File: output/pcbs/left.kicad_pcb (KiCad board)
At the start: 2 copper layers, 123.1 x 95.2 mm, 40 parts

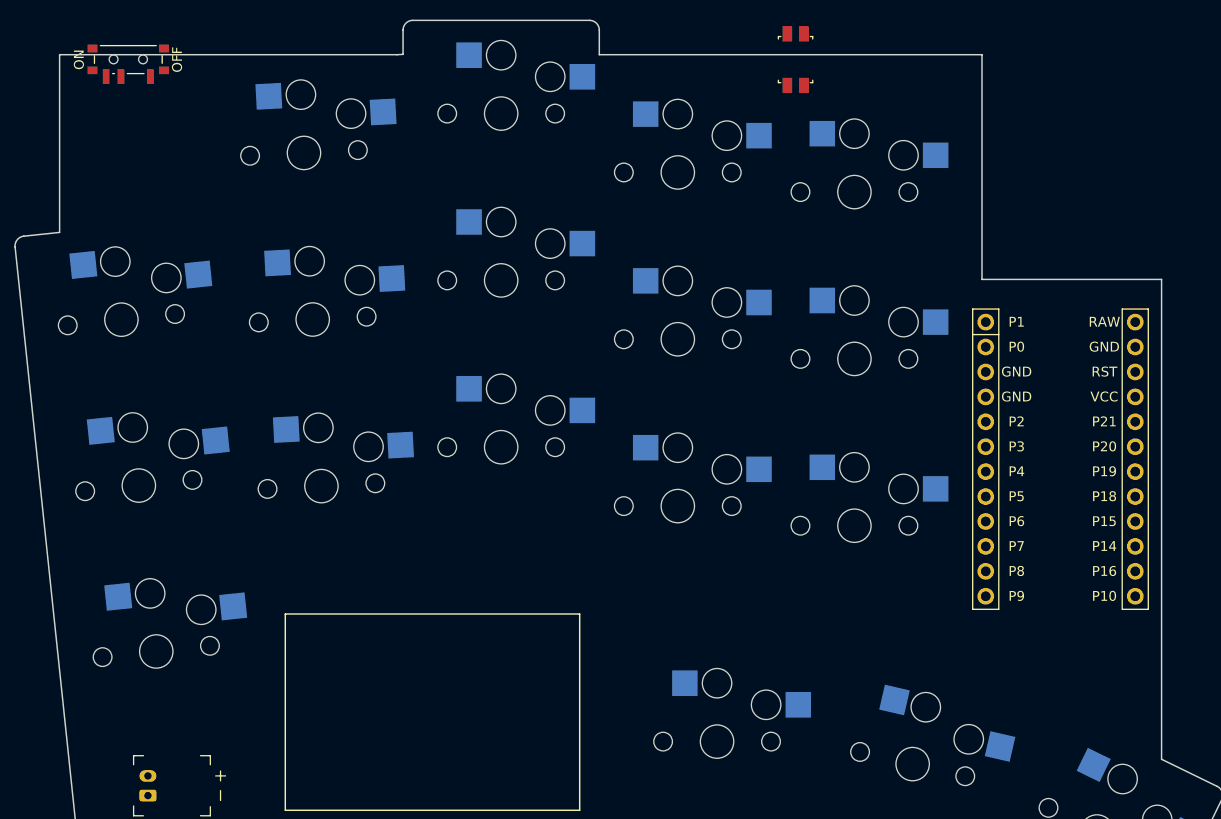
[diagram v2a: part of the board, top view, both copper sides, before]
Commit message: More detailed outlines of power, reset
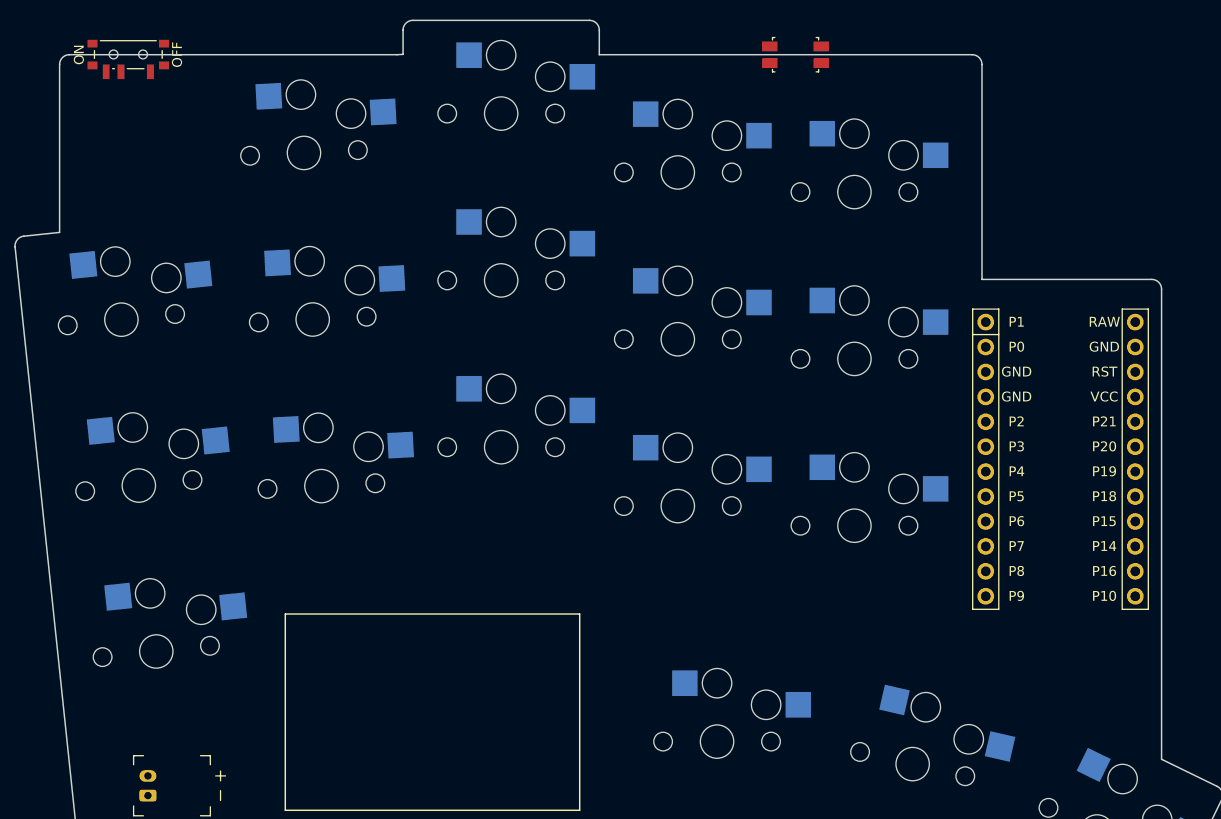
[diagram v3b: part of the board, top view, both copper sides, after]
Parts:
- moved PWR1 0.50 mm to (-2.85, -60.8)
- moved RST1 0.50 mm to (65.1, -60.8), turned to 0 degrees
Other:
- outline, holes or cut-outs redrawn
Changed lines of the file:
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@@
   (footprint "ceoloide:reset_switch_smd_side"
     (layer "F.Cu")
-    (at 65.1483667 -60.315708799999996 90)
+    (at 65.1483667 -60.815708799999996 0)
     (property "Reference" "RST1"
-      (at 0 0 90)
+      (at 0 0 0)
       (layer "F.SilkS")
       hide
@@
     (fp_line (start 1.3 -2.75) (end 1.3 -1.75) (stroke (width 0.1) (type solid)) (layer "Dwgs.User"))
     (fp_line (start 2.35 -1.75) (end 2.35 1.75) (stroke (width 0.1) (type solid)) (layer "Dwgs.User"))
-    (pad "1" smd rect (at 2.625 -0.85 270) (size 1.55 1) (layers "F.Cu" "F.Paste" "F.Mask") (net 3 "GND"))
-    (pad "2" smd rect (at 2.625 0.85 270) (size 1.55 1) (layers "F.Cu" "F.Paste" "F.Mask") (net 77 "RST"))
-    (pad "3" smd rect (at -2.625 -0.85 270) (size 1.55 1) (layers "F.Cu" "F.Paste" "F.Mask") (net 3 "GND"))
-    (pad "4" smd rect (at -2.625 0.85 270) (size 1.55 1) (layers "F.Cu" "F.Paste" "F.Mask") (net 77 "RST"))
+    (pad "1" smd rect (at 2.625 -0.85 180) (size 1.55 1) (layers "F.Cu" "F.Paste" "F.Mask") (net 3 "GND"))
+    (pad "2" smd rect (at 2.625 0.85 180) (size 1.55 1) (layers "F.Cu" "F.Paste" "F.Mask") (net 77 "RST"))
+    (pad "3" smd rect (at -2.625 -0.85 180) (size 1.55 1) (layers "F.Cu" "F.Paste" "F.Mask") (net 3 "GND"))
+    (pad "4" smd rect (at -2.625 0.85 180) (size 1.55 1) (layers "F.Cu" "F.Paste" "F.Mask") (net 77 "RST"))
     (fp_line (start -2.35 -1.5) (end -2.35 -1.75) (stroke (width 0.1) (type solid)) (layer "F.SilkS"))
     (fp_line (start -2.35 1.5) (end -2.35 1.75) (stroke (width 0.1) (type solid)) (layer "F.SilkS"))
@@
   (footprint "ceoloide:power_switch_smd_side"
     (layer "F.Cu")
-    (at -2.851633300000003 -60.315708799999996 90)
+    (at -2.851633300000003 -60.815708799999996 90)
     (property "Reference" "PWR1"
       (at -3.6 0 0)
@@
 (gr_line (start 108.1213601 13.751844899999998) (end 102.4483666 10.984941108545385) (layer Edge.Cuts) (stroke (width 0.15) (type default)))
 (gr_line (start 24.54726792343898 -60.815708799999996) (end 25.148366699999997 -60.84721104908856) (layer Edge.Cuts) (stroke (width 0.15) (type default)))
-(gr_line (start 84.1483666 -37.9157089) (end 102.4483666 -37.9157089) (layer Edge.Cuts) (stroke (width 0.15) (type default)))
-(gr_line (start 102.4483666 10.984941108545385) (end 102.4483666 -37.9157089) (layer Edge.Cuts) (stroke (width 0.15) (type default)))
+(gr_line (start 84.1483667 -37.9157089) (end 101.4483666 -37.9157089) (layer Edge.Cuts) (stroke (width 0.15) (type default)))
+(gr_line (start 102.4483666 10.984941108545385) (end 102.4483666 -36.9157089) (layer Edge.Cuts) (stroke (width 0.15) (type default)))
+(gr_arc (start 102.4483666 -36.9157089) (mid 102.1554734 -37.6228157) (end 101.4483666 -37.9157089) (layer Edge.Cuts) (stroke (width 0.15) (type default)))
 (gr_line (start -7.851633400000004 18.6842912) (end -8.1682351 17.9521569) (layer Edge.Cuts) (stroke (width 0.15) (type default)))
-(gr_line (start -9.851633300000003 -42.7041617200161) (end -9.851633300000003 -60.815708799999996) (layer Edge.Cuts) (stroke (width 0.15) (type default)))
-(gr_line (start -9.851633300000003 -60.815708799999996) (end 24.54726792343898 -60.815708799999996) (layer Edge.Cuts) (stroke (width 0.15) (type default)))
-(gr_line (start 45.148366599999996 -60.815708799999996) (end 84.1483667 -60.815708799999996) (layer Edge.Cuts) (stroke (width 0.15) (type default)))
-(gr_line (start 84.1483667 -60.815708799999996) (end 84.1483666 -37.9157089) (layer Edge.Cuts) (stroke (width 0.15) (type default)))
+(gr_line (start -9.851633300000003 -42.7041617200161) (end -9.851633300000003 -59.815708799999996) (layer Edge.Cuts) (stroke (width 0.15) (type default)))
+(gr_line (start -8.851633300000003 -60.815708799999996) (end 24.54726792343898 -60.815708799999996) (layer Edge.Cuts) (stroke (width 0.15) (type default)))
+(gr_line (start 45.148366599999996 -60.815708799999996) (end 83.1483667 -60.815708799999996) (layer Edge.Cuts) (stroke (width 0.15) (type default)))
+(gr_line (start 84.1483667 -59.815708799999996) (end 84.1483667 -37.9157089) (layer Edge.Cuts) (stroke (width 0.15) (type default)))
+(gr_arc (start -8.851633300000003 -60.815708799999996) (mid -9.558740100000003 -60.522815599999994) (end -9.851633300000003 -59.815708799999996) (layer Edge.Cuts) (stroke (width 0.15) (type default)))
+(gr_arc (start 84.1483667 -59.815708799999996) (mid 83.8554735 -60.522815599999994) (end 83.1483667 -60.815708799999996) (layer Edge.Cuts) (stroke (width 0.15) (type default)))
 (gr_line (start 13.148366599999996 -3.8157087999999995) (end 13.148366599999996 16.1842912) (layer F.SilkS) (stroke (width 0.15) (type default)))
 (gr_line (start 13.148366599999996 16.1842912) (end 43.148366599999996 16.1842912) (layer F.SilkS) (stroke (width 0.15) (type default)))

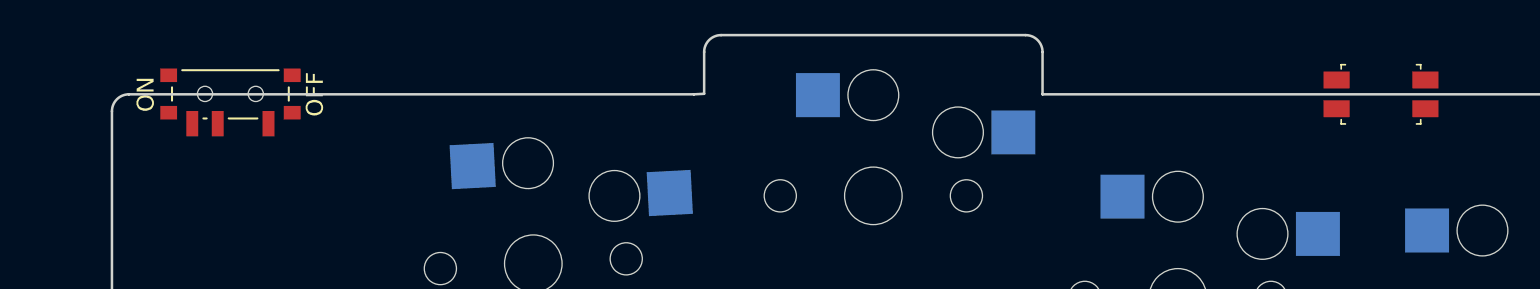
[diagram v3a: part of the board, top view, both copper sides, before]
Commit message: Adjust placement of switches
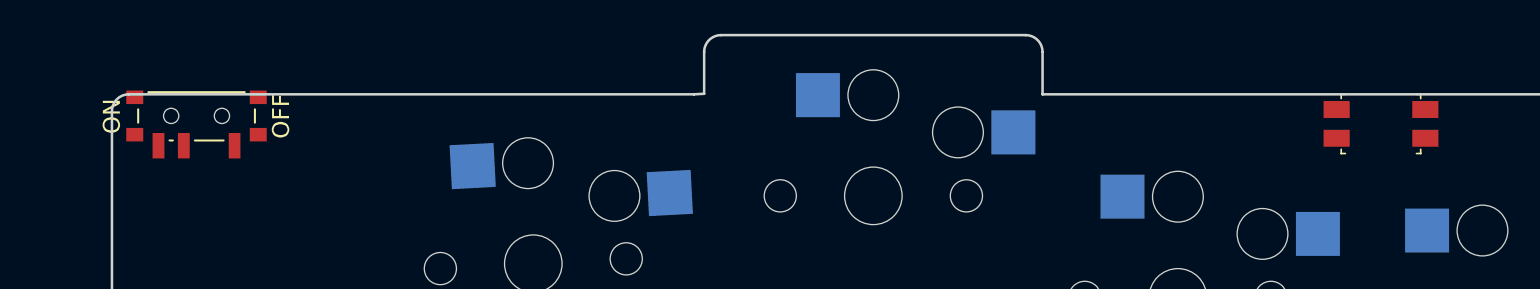
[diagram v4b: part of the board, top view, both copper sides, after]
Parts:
- moved PWR1 2.39 mm to (-4.85, -59.5)
- moved RST1 1.75 mm to (65.1, -59.1)
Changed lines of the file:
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@@
     (fp_line (start -6.29 -11.43) (end -8.95 -11.43) (layer "F.SilkS") (stroke (width 0.12) (type solid)))
-  )
-  (footprint "ceoloide:reset_switch_smd_side"
-    (layer "F.Cu")
-    (at 65.1483667 -60.815708799999996 0)
-    (property "Reference" "RST1"
-      (at 0 0 0)
-      (layer "F.SilkS")
-      hide
-      (effects (font (size 1 1) (thickness 0.15)))
-    )
-    (attr smd)
-    (fp_line (start -2.35 -1.75) (end -2.35 1.75) (stroke (width 0.1) (type solid)) (layer "Dwgs.User"))
-    (fp_line (start -2.35 -1.75) (end 2.35 -1.75) (stroke (width 0.1) (type solid)) (layer "Dwgs.User"))
-    (fp_line (start -2.35 1.75) (end 2.35 1.75) (stroke (width 0.1) (type solid)) (layer "Dwgs.User"))
-    (fp_line (start -1.3 -2.75) (end -1.3 -1.75) (stroke (width 0.1) (type solid)) (layer "Dwgs.User"))
-    (fp_line (start -1.3 -2.75) (end 1.3 -2.75) (stroke (width 0.1) (type solid)) (layer "Dwgs.User"))
-    (fp_line (start 1.3 -2.75) (end 1.3 -1.75) (stroke (width 0.1) (type solid)) (layer "Dwgs.User"))
-    (fp_line (start 2.35 -1.75) (end 2.35 1.75) (stroke (width 0.1) (type solid)) (layer "Dwgs.User"))
-    (pad "1" smd rect (at 2.625 -0.85 180) (size 1.55 1) (layers "F.Cu" "F.Paste" "F.Mask") (net 3 "GND"))
-    (pad "2" smd rect (at 2.625 0.85 180) (size 1.55 1) (layers "F.Cu" "F.Paste" "F.Mask") (net 77 "RST"))
-    (pad "3" smd rect (at -2.625 -0.85 180) (size 1.55 1) (layers "F.Cu" "F.Paste" "F.Mask") (net 3 "GND"))
-    (pad "4" smd rect (at -2.625 0.85 180) (size 1.55 1) (layers "F.Cu" "F.Paste" "F.Mask") (net 77 "RST"))
-    (fp_line (start -2.35 -1.5) (end -2.35 -1.75) (stroke (width 0.1) (type solid)) (layer "F.SilkS"))
-    (fp_line (start -2.35 1.5) (end -2.35 1.75) (stroke (width 0.1) (type solid)) (layer "F.SilkS"))
-    (fp_line (start -2.1 -1.75) (end -2.35 -1.75) (stroke (width 0.1) (type solid)) (layer "F.SilkS"))
-    (fp_line (start -2.1 1.75) (end -2.35 1.75) (stroke (width 0.1) (type solid)) (layer "F.SilkS"))
-    (fp_line (start 2.1 -1.75) (end 2.35 -1.75) (stroke (width 0.1) (type solid)) (layer "F.SilkS"))
-    (fp_line (start 2.1 1.75) (end 2.35 1.75) (stroke (width 0.1) (type solid)) (layer "F.SilkS"))
-    (fp_line (start 2.35 -1.5) (end 2.35 -1.75) (stroke (width 0.1) (type solid)) (layer "F.SilkS"))
-    (fp_line (start 2.35 1.5) (end 2.35 1.75) (stroke (width 0.1) (type solid)) (layer "F.SilkS"))
   )
   (footprint "ceoloide:power_switch_smd_side"
     (layer "F.Cu")
-    (at -2.851633300000003 -60.815708799999996 90)
+    (at -4.851633300000003 -59.5157088 90)
     (property "Reference" "PWR1"
       (at -3.6 0 0)
@@
     (pad "" np_thru_hole circle (at 0.025 1.5 180) (size 0.9 0.9) (drill 0.9) (layers "*.Cu" "*.Mask"))
   )
+  (footprint "ceoloide:reset_switch_smd_side"
+    (layer "F.Cu")
+    (at 65.1483667 -59.065708799999996 0)
+    (property "Reference" "RST1"
+      (at 0 0 0)
+      (layer "F.SilkS")
+      hide
+      (effects (font (size 1 1) (thickness 0.15)))
+    )
+    (attr smd)
+    (fp_line (start -2.35 -1.75) (end -2.35 1.75) (stroke (width 0.1) (type solid)) (layer "Dwgs.User"))
+    (fp_line (start -2.35 -1.75) (end 2.35 -1.75) (stroke (width 0.1) (type solid)) (layer "Dwgs.User"))
+    (fp_line (start -2.35 1.75) (end 2.35 1.75) (stroke (width 0.1) (type solid)) (layer "Dwgs.User"))
+    (fp_line (start -1.3 -2.75) (end -1.3 -1.75) (stroke (width 0.1) (type solid)) (layer "Dwgs.User"))
+    (fp_line (start -1.3 -2.75) (end 1.3 -2.75) (stroke (width 0.1) (type solid)) (layer "Dwgs.User"))
+    (fp_line (start 1.3 -2.75) (end 1.3 -1.75) (stroke (width 0.1) (type solid)) (layer "Dwgs.User"))
+    (fp_line (start 2.35 -1.75) (end 2.35 1.75) (stroke (width 0.1) (type solid)) (layer "Dwgs.User"))
+    (pad "1" smd rect (at 2.625 -0.85 180) (size 1.55 1) (layers "F.Cu" "F.Paste" "F.Mask") (net 3 "GND"))
+    (pad "2" smd rect (at 2.625 0.85 180) (size 1.55 1) (layers "F.Cu" "F.Paste" "F.Mask") (net 77 "RST"))
+    (pad "3" smd rect (at -2.625 -0.85 180) (size 1.55 1) (layers "F.Cu" "F.Paste" "F.Mask") (net 3 "GND"))
+    (pad "4" smd rect (at -2.625 0.85 180) (size 1.55 1) (layers "F.Cu" "F.Paste" "F.Mask") (net 77 "RST"))
+    (fp_line (start -2.35 -1.5) (end -2.35 -1.75) (stroke (width 0.1) (type solid)) (layer "F.SilkS"))
+    (fp_line (start -2.35 1.5) (end -2.35 1.75) (stroke (width 0.1) (type solid)) (layer "F.SilkS"))
+    (fp_line (start -2.1 -1.75) (end -2.35 -1.75) (stroke (width 0.1) (type solid)) (layer "F.SilkS"))
+    (fp_line (start -2.1 1.75) (end -2.35 1.75) (stroke (width 0.1) (type solid)) (layer "F.SilkS"))
+    (fp_line (start 2.1 -1.75) (end 2.35 -1.75) (stroke (width 0.1) (type solid)) (layer "F.SilkS"))
+    (fp_line (start 2.1 1.75) (end 2.35 1.75) (stroke (width 0.1) (type solid)) (layer "F.SilkS"))
+    (fp_line (start 2.35 -1.5) (end 2.35 -1.75) (stroke (width 0.1) (type solid)) (layer "F.SilkS"))
+    (fp_line (start 2.35 1.5) (end 2.35 1.75) (stroke (width 0.1) (type solid)) (layer "F.SilkS"))
+  )
     (footprint "ceoloide:battery_connector_jst_ph_2"

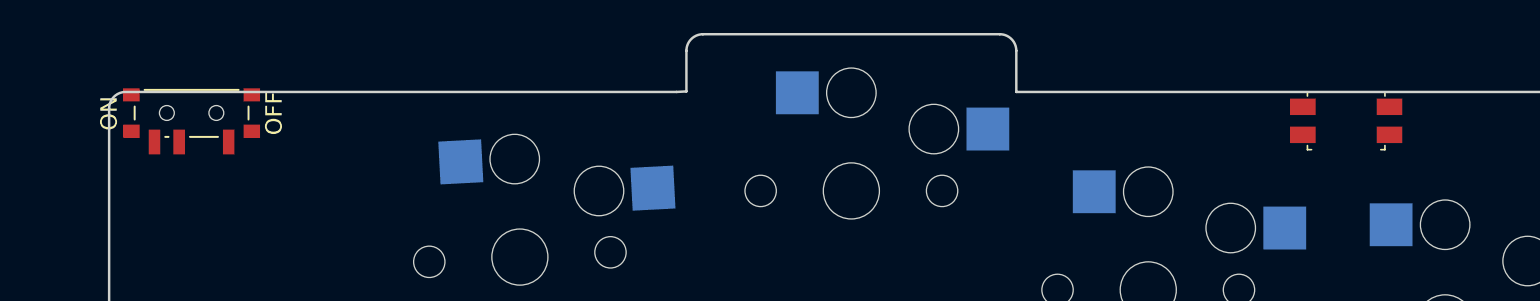
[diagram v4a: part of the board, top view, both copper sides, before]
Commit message: Adjust horizontally
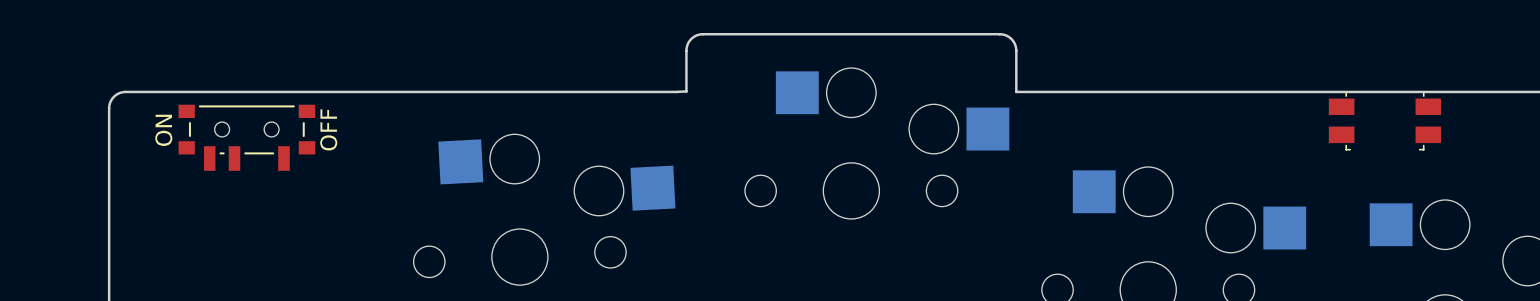
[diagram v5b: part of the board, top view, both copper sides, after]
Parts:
- moved PWR1 3.50 mm to (-1.50, -58.5)
- moved RST1 2.35 mm to (67.5, -59.1)
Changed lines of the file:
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@@
   (footprint "ceoloide:power_switch_smd_side"
     (layer "F.Cu")
-    (at -4.851633300000003 -59.5157088 90)
+    (at -1.5016333000000017 -58.5157088 90)
     (property "Reference" "PWR1"
       (at -3.6 0 0)
@@
   (footprint "ceoloide:reset_switch_smd_side"
     (layer "F.Cu")
-    (at 65.1483667 -59.065708799999996 0)
+    (at 67.49836669999999 -59.065708799999996 0)
     (property "Reference" "RST1"
       (at 0 0 0)

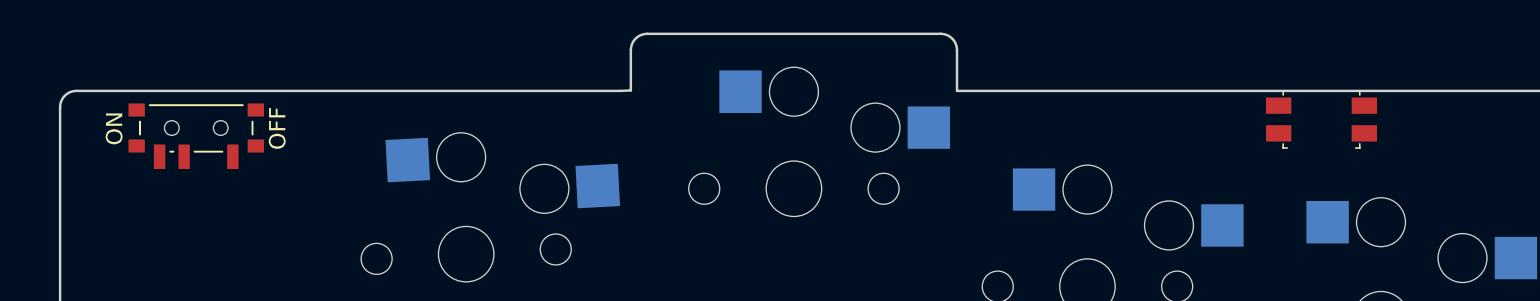
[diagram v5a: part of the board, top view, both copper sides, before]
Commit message: Adjust power/reset a little more
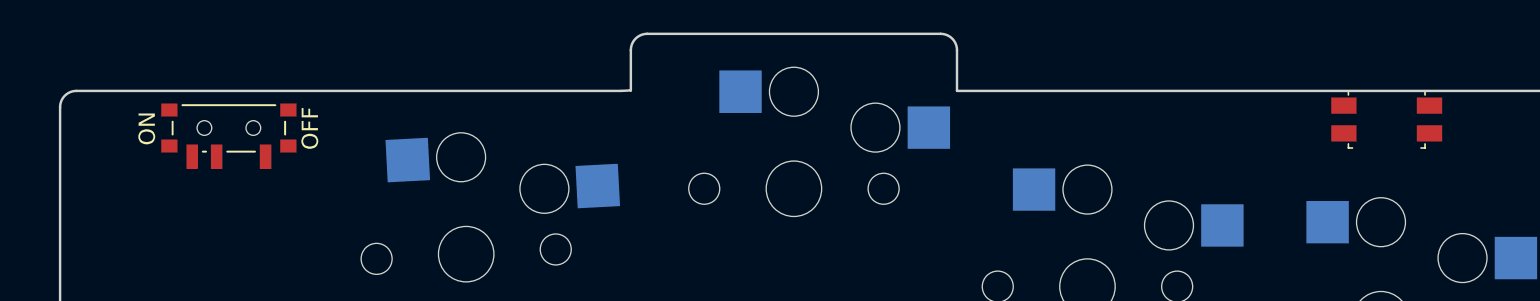
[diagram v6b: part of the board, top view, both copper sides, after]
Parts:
- moved RST1 4.00 mm to (71.5, -59.1)
- moved PWR1 2.00 mm to (0.50, -58.5)
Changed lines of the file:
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@@
   (footprint "ceoloide:power_switch_smd_side"
     (layer "F.Cu")
-    (at -1.5016333000000017 -58.5157088 90)
+    (at 0.4983666999999983 -58.5157088 90)
     (property "Reference" "PWR1"
       (at -3.6 0 0)
@@
   (footprint "ceoloide:reset_switch_smd_side"
     (layer "F.Cu")
-    (at 67.49836669999999 -59.065708799999996 0)
+    (at 71.49836669999999 -59.065708799999996 0)
     (property "Reference" "RST1"
       (at 0 0 0)
